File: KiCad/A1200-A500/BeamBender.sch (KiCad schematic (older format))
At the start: 32 parts, among them J1 4-1734742-0, J2 HDMI_A_1.4, J3 STX-3501-3N, J4 Phoenix_Contact, U1 LM1117-3.3, U3 ADV7513BSWZ, X1 Abracon ASE-27.000MHZ-L-R-T

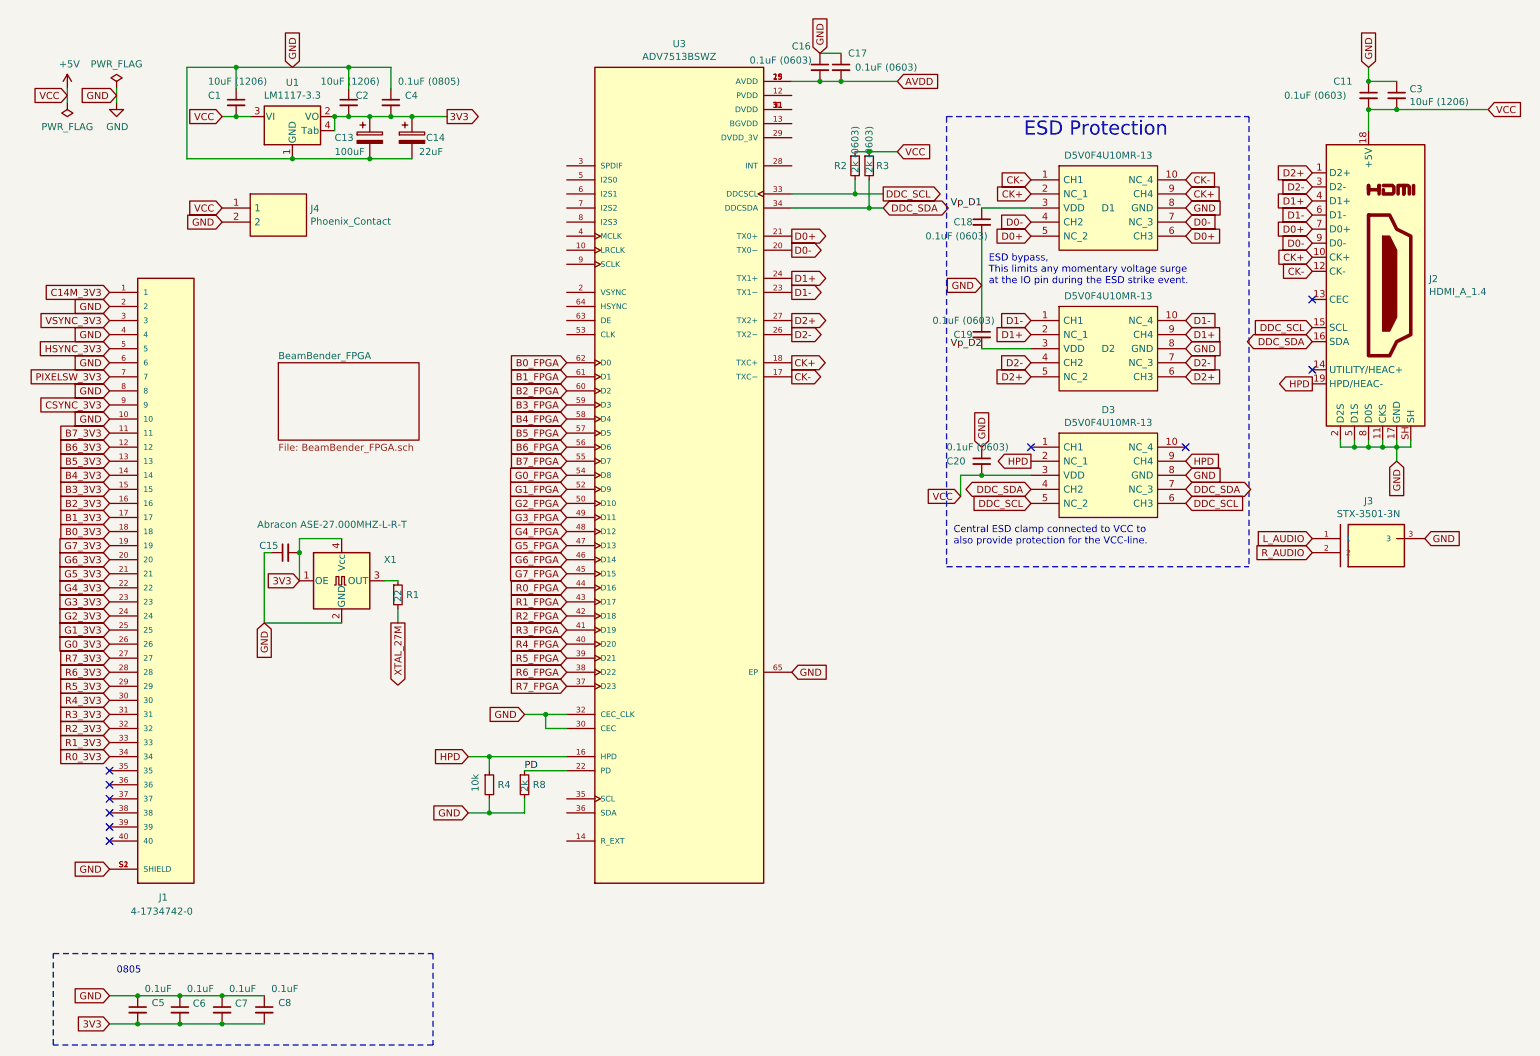
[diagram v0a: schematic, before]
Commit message: more place and route done
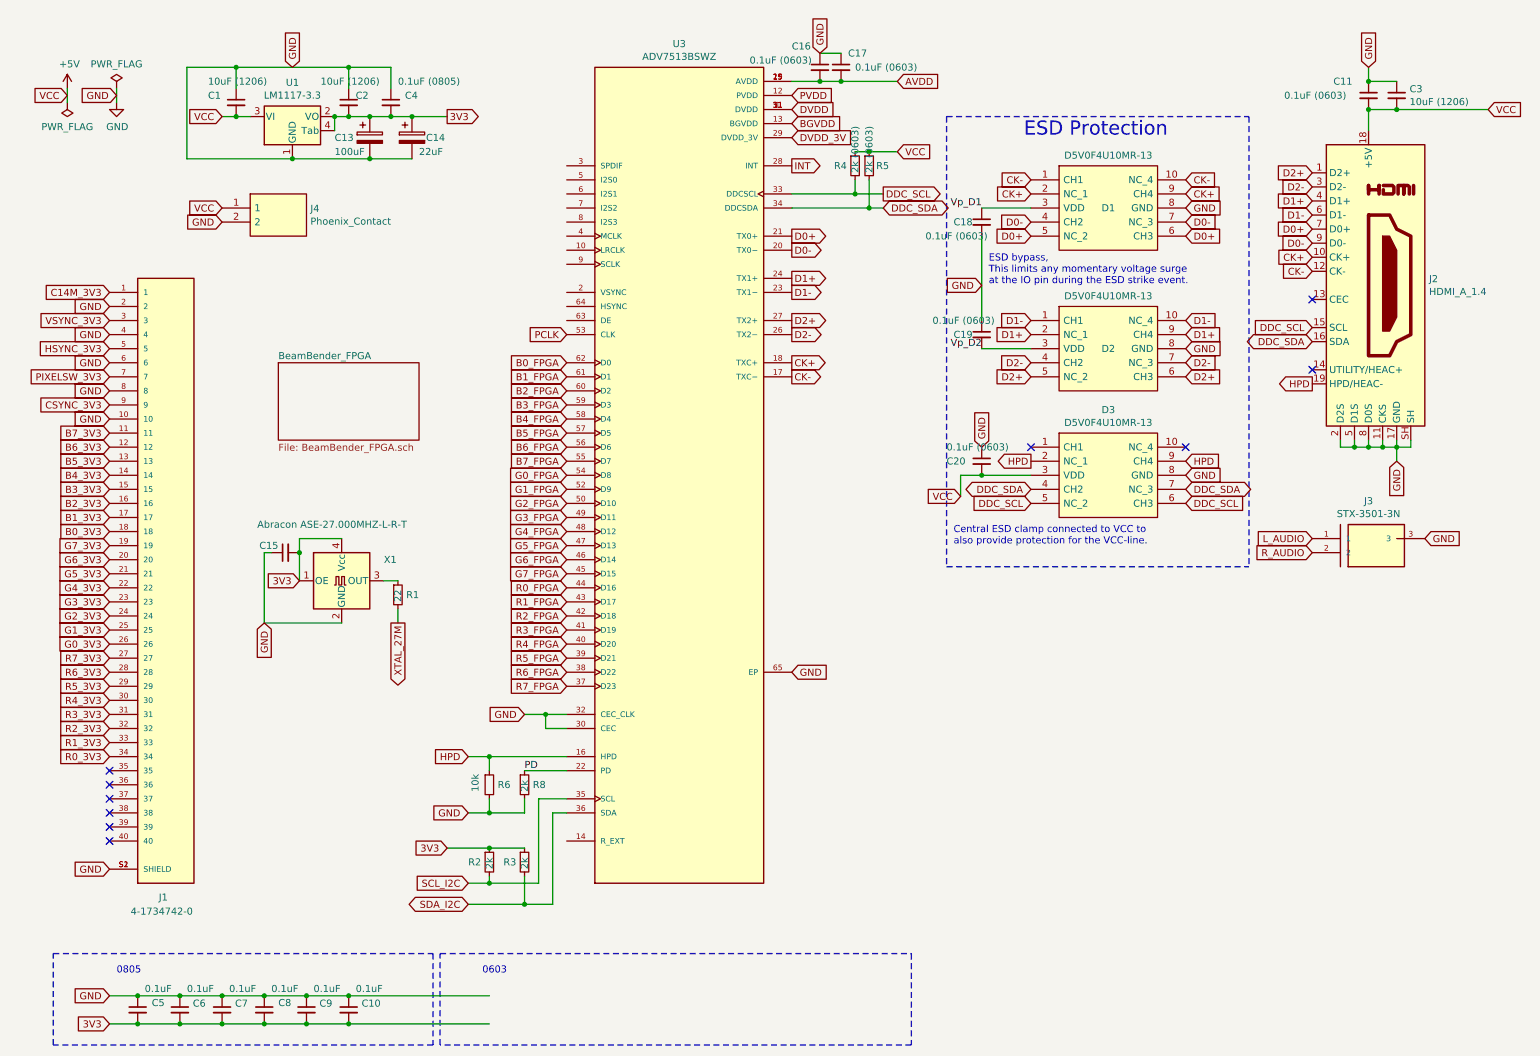
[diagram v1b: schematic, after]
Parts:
- added C10, C9: 0.1uF, Capacitor_SMD:C_0805_2012Metric_Pad1.18x1.45mm_HandSolder, symbol Device:C_Small
- added R2, R3: 2k, Resistor_SMD:R_0603_1608Metric_Pad0.98x0.95mm_HandSolder, symbol Device:R_Small
- renumbered R2 to R4, R3 to R5, R4 to R6
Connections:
- net 3V3: now also C10.2, C9.2, R2.1, R3.1
- net GND: now also C10.1, C9.1
- net DVDD: now reaches U3.1 (DVDD), U3.11 (DVDD), U3.31 (DVDD), U3.51 (DVDD)
- net PVDD: now reaches U3.12 (PVDD)
- net BGVDD: now reaches U3.13 (BGVDD)
- net INT: now reaches U3.28 (INT)
- net DVDD_3V: now reaches U3.29 (DVDD_3V)
- net SCL_I2C: now reaches U3.35 (SCL)
- net SCL_I2C: now also R2.2
- net SDA_I2C: now reaches U3.36 (SDA)
- net SDA_I2C: now also R3.2
- net PCLK: now reaches U3.53 (CLK)
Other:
- note added: "0603"
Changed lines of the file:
@@
 Text GLabel 8800 3600 2    50   Input ~ 0
 HPD
-Text GLabel 3700 5700 0    50   Input ~ 0
-HPD
-$Comp
-L Device:R_Small R4
-U 1 1 652DC9C5
-P 3850 5900
-F 0 "R4" H 3909 5900 50  0000 L CNN
-F 1 "10k" V 3750 5850 50  0000 L CNN
-F 2 "Resistor_SMD:R_0603_1608Metric_Pad0.98x0.95mm_HandSolder" H 3850 5900 50  0001 C CNN
-F 3 "~" H 3850 5900 50  0001 C CNN
-	1    3850 5900
-	1    0    0    -1
-$EndComp
-Text GLabel 3700 6100 0    50   Input ~ 0
-GND
-Wire Wire Line
-	3700 5700 3850 5700
-$Comp
-L Device:R_Small R8
-U 1 1 6531102F
-P 4100 5900
-F 0 "R8" H 4159 5900 50  0000 L CNN
-F 1 "2k" V 4100 5850 50  0000 L CNN
-F 2 "Resistor_SMD:R_0603_1608Metric_Pad0.98x0.95mm_HandSolder" H 4100 5900 50  0001 C CNN
-F 3 "~" H 4100 5900 50  0001 C CNN
-	1    4100 5900
-	1    0    0    -1
-$EndComp
-Wire Wire Line
-	4100 5800 4400 5800
-Text Label 4100 5800 0    50   ~ 0
-PD
-Wire Wire Line
-	4100 6100 3850 6100
-Wire Wire Line
-	3850 6100 3850 6000
-Wire Wire Line
-	3700 6100 3850 6100
-Connection ~ 3850 6100
-Wire Wire Line
-	4100 6000 4100 6100
-Wire Wire Line
-	4400 5700 3850 5700
-Wire Wire Line
-	3850 5700 3850 5800
-Connection ~ 3850 5700
 Text GLabel 4100 5400 0    50   Input ~ 0
 GND
@@
 GND
 $Comp
-L Device:R_Small R2
+L Device:R_Small R4
 U 1 1 6532D8B1
 P 6450 1500
-F 0 "R2" H 6300 1500 50  0000 L CNN
+F 0 "R4" H 6300 1500 50  0000 L CNN
 F 1 "2k  (0603)" V 6450 1450 50  0000 L CNN
 F 2 "Resistor_SMD:R_0603_1608Metric_Pad0.98x0.95mm_HandSolder" H 6450 1500 50  0001 C CNN
@@
 Connection ~ 3300 1150
 $Comp
-L Device:R_Small R3
+L Device:R_Small R5
 U 1 1 6532BC2D
 P 6550 1500
-F 0 "R3" H 6600 1500 50  0000 L CNN
+F 0 "R5" H 6600 1500 50  0000 L CNN
 F 1 "2k  (0603)" V 6550 1450 50  0000 L CNN
 F 2 "Resistor_SMD:R_0603_1608Metric_Pad0.98x0.95mm_HandSolder" H 6550 1500 50  0001 C CNN
@@
 	1950 7600 2250 7600
 Connection ~ 1950 7600
+Text GLabel 3700 6600 0    50   Input ~ 0
+SCL_I2C
+Connection ~ 3850 5700
+Wire Wire Line
+	3850 5700 3850 5800
+Wire Wire Line
+	4400 5700 3850 5700
+Wire Wire Line
+	4100 6000 4100 6100
+Connection ~ 3850 6100
+Wire Wire Line
+	3700 6100 3850 6100
+Wire Wire Line
+	3850 6100 3850 6000
+Wire Wire Line
+	4100 6100 3850 6100
+Text Label 4100 5800 0    50   ~ 0
+PD
+Wire Wire Line
+	4100 5800 4400 5800
+$Comp
+L Device:R_Small R8
+U 1 1 6531102F
+P 4100 5900
+F 0 "R8" H 4159 5900 50  0000 L CNN
+F 1 "2k" V 4100 5850 50  0000 L CNN
+F 2 "Resistor_SMD:R_0603_1608Metric_Pad0.98x0.95mm_HandSolder" H 4100 5900 50  0001 C CNN
+F 3 "~" H 4100 5900 50  0001 C CNN
+	1    4100 5900
+	1    0    0    -1
+$EndComp
+Wire Wire Line
+	3700 5700 3850 5700
+Text GLabel 3700 6100 0    50   Input ~ 0
+GND
+$Comp
+L Device:R_Small R6
+U 1 1 652DC9C5
+P 3850 5900
+F 0 "R6" H 3909 5900 50  0000 L CNN
+F 1 "10k" V 3750 5850 50  0000 L CNN
+F 2 "Resistor_SMD:R_0603_1608Metric_Pad0.98x0.95mm_HandSolder" H 3850 5900 50  0001 C CNN
+F 3 "~" H 3850 5900 50  0001 C CNN
+	1    3850 5900
+	1    0    0    -1
+$EndComp
+Text GLabel 3700 5700 0    50   Input ~ 0
+HPD
+Wire Wire Line
+	3700 6600 3850 6600
+Wire Wire Line
+	4200 6000 4400 6000
+Wire Wire Line
+	4200 6000 4200 6600
+Text GLabel 3700 6750 0    50   BiDi ~ 0
+SDA_I2C
+Wire Wire Line
+	3700 6750 4100 6750
+Wire Wire Line
+	4300 6750 4300 6100
+Wire Wire Line
+	4300 6100 4400 6100
+$Comp
+L Device:R_Small R2
+U 1 1 655C6F45
+P 3850 6450
+F 0 "R2" H 3700 6450 50  0000 L CNN
+F 1 "2k" V 3850 6400 50  0000 L CNN
+F 2 "Resistor_SMD:R_0603_1608Metric_Pad0.98x0.95mm_HandSolder" H 3850 6450 50  0001 C CNN
+F 3 "~" H 3850 6450 50  0001 C CNN
+	1    3850 6450
+	1    0    0    -1
+$EndComp
+Text GLabel 3550 6350 0    50   Input ~ 0
+3V3
+Wire Wire Line
+	3550 6350 3850 6350
+Wire Wire Line
+	3850 6550 3850 6600
+Connection ~ 3850 6600
+Wire Wire Line
+	3850 6600 4200 6600
+$Comp
+L Device:R_Small R3
+U 1 1 655D3232
+P 4100 6450
+F 0 "R3" H 3950 6450 50  0000 L CNN
+F 1 "2k" V 4100 6400 50  0000 L CNN
+F 2 "Resistor_SMD:R_0603_1608Metric_Pad0.98x0.95mm_HandSolder" H 4100 6450 50  0001 C CNN
+F 3 "~" H 4100 6450 50  0001 C CNN
+	1    4100 6450
+	1    0    0    -1
+$EndComp
+Wire Wire Line
+	3850 6350 4100 6350
+Connection ~ 3850 6350
+Wire Wire Line
+	4100 6550 4100 6750
+Connection ~ 4100 6750
+Wire Wire Line
+	4100 6750 4300 6750
+Connection ~ 2250 7400
+Connection ~ 2250 7600
+Wire Notes Line
+	3500 7100 6850 7100
+Wire Notes Line
+	6850 7100 6850 7750
+Wire Notes Line
+	6850 7750 3500 7750
+Wire Notes Line
+	3500 7750 3500 7100
+Text Notes 3800 7250 0    50   ~ 0
+0603
+Wire Wire Line
+	2250 7400 2550 7400
+Wire Wire Line
+	2250 7600 2550 7600
+$Comp
+L Device:C_Small C9
+U 1 1 6560730E
+P 2550 7500
+F 0 "C9" H 2642 7546 50  0000 L CNN
+F 1 "0.1uF" H 2600 7650 50  0000 L CNN
+F 2 "Capacitor_SMD:C_0805_2012Metric_Pad1.18x1.45mm_HandSolder" H 2550 7500 50  0001 C CNN
+F 3 "~" H 2550 7500 50  0001 C CNN
+	1    2550 7500
+	1    0    0    -1
+$EndComp
+Connection ~ 2550 7400
+Wire Wire Line
+	2550 7400 2850 7400
+Connection ~ 2550 7600
+Wire Wire Line
+	2550 7600 2850 7600
+Text GLabel 6000 1500 2    50   Output ~ 0
+INT
+Text GLabel 6000 1000 2    50   Input ~ 0
+PVDD
+Text GLabel 6000 1100 2    50   Input ~ 0
+DVDD
+Text GLabel 6000 1300 2    50   Input ~ 0
+DVDD_3V
+Text GLabel 6000 1200 2    50   Input ~ 0
+BGVDD
+$Comp
+L Device:C_Small C10
+U 1 1 6563C1E1
+P 2850 7500
+F 0 "C10" H 2942 7546 50  0000 L CNN
+F 1 "0.1uF" H 2900 7650 50  0000 L CNN
+F 2 "Capacitor_SMD:C_0805_2012Metric_Pad1.18x1.45mm_HandSolder" H 2850 7500 50  0001 C CNN
+F 3 "~" H 2850 7500 50  0001 C CNN
+	1    2850 7500
+	1    0    0    -1
+$EndComp
+Connection ~ 2850 7400
+Wire Wire Line
+	2850 7400 3850 7400
+Connection ~ 2850 7600
+Wire Wire Line
+	2850 7600 3850 7600
+Text GLabel 4400 2700 0    50   Input ~ 0
+PCLK
 $EndSCHEMATC
